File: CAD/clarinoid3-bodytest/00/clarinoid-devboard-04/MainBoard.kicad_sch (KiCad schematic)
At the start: 27 parts, among them J12 I2C HEADER main to LH, J13 ENC_HEADER main to lh, J15 StereoPot_SW_CommonAudioGND, J16 AudioOut, J19 header_ws2812 main to LH, J7 I2C HEADER main to PITCH, J9 OLED_HEADER, SW1 sw_program, U2 APCI0108-P001A Teensy_4.0_Mic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, U3 Micromod outline

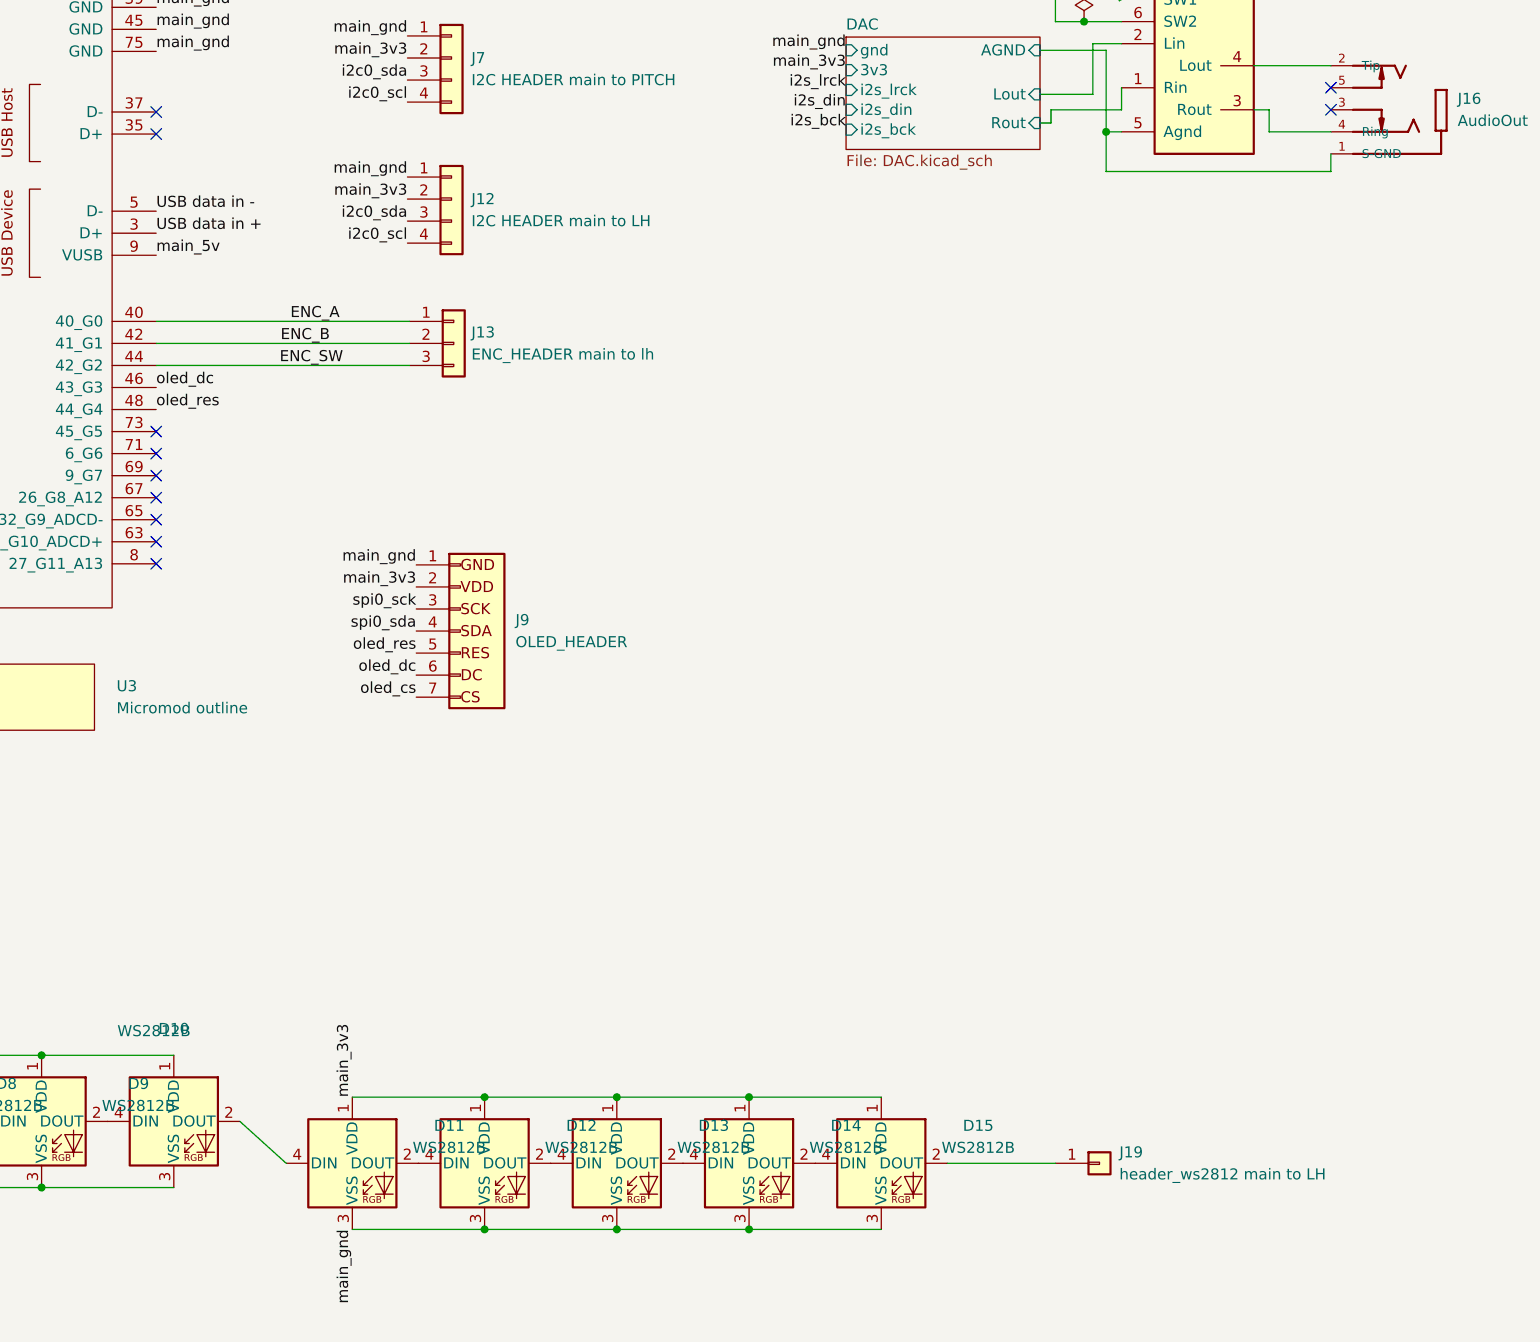
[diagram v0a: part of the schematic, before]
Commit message: adding a hardware layout sketch to the midi performer device PCB progress on the clarinoid3 body
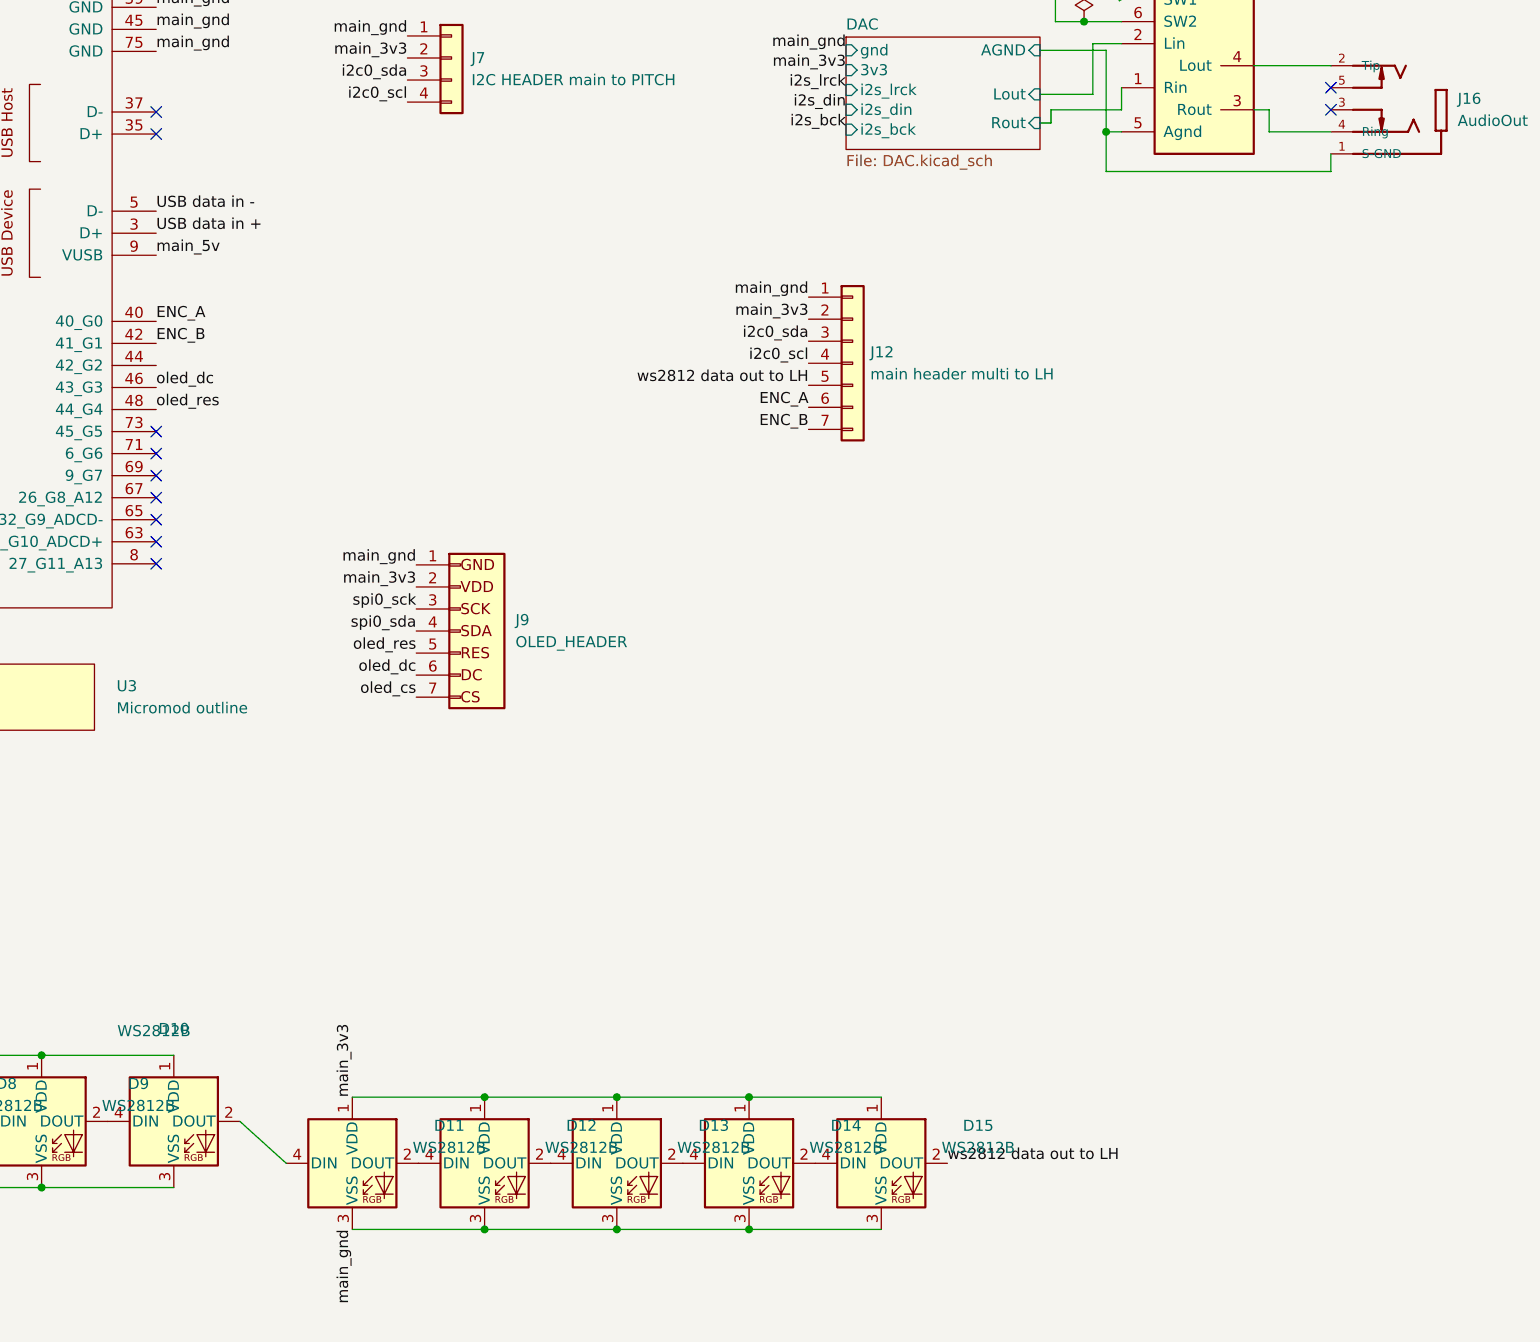
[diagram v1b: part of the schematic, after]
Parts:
- removed J12: I2C HEADER main to LH, Connector_PinHeader_2.00mm:PinHeader_1x04_P2.00mm_Vertical, symbol Connector_Generic:Conn_01x04
- removed J13: ENC_HEADER main to lh, Connector_PinHeader_2.00mm:PinHeader_1x03_P2.00mm_Vertical, symbol Connector_Generic:Conn_01x03
- removed J19: header_ws2812 main to LH, Connector_PinHeader_2.00mm:PinHeader_1x01_P2.00mm_Vertical, symbol Connector_Generic:Conn_01x01
- added J12: main header multi to LH, Connector_PinHeader_2.54mm:PinHeader_1x07_P2.54mm_Vertical, symbol Connector_Generic:Conn_01x07
- H4, H5, H6, H7: footprint clarinoid2:Wurth Elektronik Reverse SMD Spacer M3 -> MountingHole:MountingHole_2.7mm_M2.5
- J7: footprint Connector_PinHeader_2.00mm:PinHeader_1x04_P2.00mm_Vertical -> Connector_PinHeader_2.54mm:PinHeader_1x04_P2.54mm_Vertical
- J9: footprint Connector_PinHeader_2.00mm:PinHeader_1x07_P2.00mm_Vertical -> Connector_PinHeader_2.54mm:PinHeader_1x07_P2.54mm_Vertical
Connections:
- net ENC_A: now also J12.6 (Pin_6)
- net ENC_B: now also J12.7 (Pin_7)
- net i2c0_scl: now also J12.4 (Pin_4)
- net i2c0_sda: now also J12.3 (Pin_3)
- net main_3v3: now also J12.2 (Pin_2)
- net main_gnd: now also J12.1 (Pin_1)
- net ws2812 data out to LH: now reaches D15.2 (DOUT)
- net ws2812 data out to LH: now also J12.5 (Pin_5)
- net ENC_SW: no longer names the net of U2.44 (42_G2)
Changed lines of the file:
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@@
-    (stroke (width 0) (type default) (color 0 0 0 0))
-  )
-  (wire (pts (xy 142.494 144.272) (xy 113.284 144.272))
     (stroke (width 0) (type default) (color 0 0 0 0))
   )
@@
     (stroke (width 0) (type default) (color 0 0 0 0))
   )
-  (wire (pts (xy 142.494 139.192) (xy 113.284 139.192))
-    (stroke (width 0) (type default) (color 0 0 0 0))
-  )
   (wire (pts (xy 37.084 90.043) (xy 37.084 93.345))
     (stroke (width 0) (type default) (color 0 0 0 0))
@@
     (stroke (width 0) (type default) (color 0 0 0 0))
   )
-  (wire (pts (xy 216.916 236.22) (xy 204.47 236.22))
-    (stroke (width 0) (type default) (color 0 0 0 0))
-  )
   (wire (pts (xy 222.758 117.348) (xy 222.758 121.92))
     (stroke (width 0) (type default) (color 0 0 0 0))
@@
   )
   (wire (pts (xy 100.076 239.014) (xy 115.316 239.014))
-    (stroke (width 0) (type default) (color 0 0 0 0))
-  )
-  (wire (pts (xy 142.494 141.732) (xy 113.284 141.732))
     (stroke (width 0) (type default) (color 0 0 0 0))
   )
@@
     (effects (font (size 1.27 1.27)) (justify left bottom))
   )
-  (label "i2c0_scl" (at 142.24 130.175 180)
+  (label "i2c0_scl" (at 188.468 144.018 180)
     (effects (font (size 1.27 1.27)) (justify right bottom))
   )
@@
     (effects (font (size 1.27 1.27)) (justify right bottom))
   )
+  (label "ws2812 data out to LH" (at 188.468 146.558 180)
+    (effects (font (size 1.27 1.27)) (justify right bottom))
+  )
   (label "i2s_bck" (at 192.786 117.094 180)
     (effects (font (size 1.27 1.27)) (justify right bottom))
@@
     (effects (font (size 1.27 1.27)) (justify right bottom))
   )
-  (label "ENC_B" (at 127.6189 141.732 0)
+  (label "ENC_A" (at 188.468 149.098 180)
+    (effects (font (size 1.27 1.27)) (justify right bottom))
+  )
+  (label "ENC_B" (at 113.284 141.732 0)
     (effects (font (size 1.27 1.27)) (justify left bottom))
   )
@@
     (effects (font (size 1.27 1.27)) (justify right bottom))
   )
-  (label "main_3v3" (at 142.24 125.095 180)
+  (label "main_3v3" (at 188.468 138.938 180)
     (effects (font (size 1.27 1.27)) (justify right bottom))
   )
@@
     (effects (font (size 1.27 1.27)) (justify left bottom))
   )
+  (label "ws2812 data out to LH" (at 204.47 236.22 0)
+    (effects (font (size 1.27 1.27)) (justify left bottom))
+  )
+  (label "ENC_B" (at 188.468 151.638 180)
+    (effects (font (size 1.27 1.27)) (justify right bottom))
+  )
   (label "main_gnd" (at 242.57 79.883 180)
     (effects (font (size 1.27 1.27)) (justify right bottom))
@@
     (effects (font (size 1.27 1.27)) (justify right bottom))
   )
-  (label "ENC_A" (at 128.7493 139.192 0)
+  (label "ENC_A" (at 113.284 139.192 0)
     (effects (font (size 1.27 1.27)) (justify left bottom))
   )
@@
     (effects (font (size 1.27 1.27)) (justify right bottom))
   )
-  (label "ENC_SW" (at 127.508 144.272 0)
-    (effects (font (size 1.27 1.27)) (justify left bottom))
-  )
   (label "main_gnd" (at 105.156 27.432 180)
     (effects (font (size 1.27 1.27)) (justify right bottom))
@@
     (effects (font (size 1.27 1.27)) (justify left bottom))
   )
-  (label "main_gnd" (at 142.24 122.555 180)
+  (label "main_gnd" (at 188.468 136.398 180)
     (effects (font (size 1.27 1.27)) (justify right bottom))
   )
@@
     (effects (font (size 1.27 1.27)) (justify right bottom))
   )
-  (label "i2c0_sda" (at 142.24 127.635 180)
+  (label "i2c0_sda" (at 188.468 141.478 180)
     (effects (font (size 1.27 1.27)) (justify right bottom))
   )
@@
       (effects (font (size 1.27 1.27)) (justify left))
     )
-    (property "Footprint" "clarinoid2:Wurth Elektronik Reverse SMD Spacer M3" (id 2) (at 170.053 61.468 0)
+    (property "Footprint" "MountingHole:MountingHole_2.7mm_M2.5" (id 2) (at 170.053 61.468 0)
       (effects (font (size 1.27 1.27)) hide)
     )
@@
       (effects (font (size 1.27 1.27)) (justify left))
     )
-    (property "Footprint" "Connector_PinHeader_2.00mm:PinHeader_1x07_P2.00mm_Vertical" (id 2) (at 148.336 174.879 0)
+    (property "Footprint" "Connector_PinHeader_2.54mm:PinHeader_1x07_P2.54mm_Vertical" (id 2) (at 148.336 174.879 0)
       (effects (font (size 1.27 1.27)) hide)
     )
@@
       (effects (font (size 1.27 1.27)) (justify left))
     )
-    (property "Footprint" "clarinoid2:Wurth Elektronik Reverse SMD Spacer M3" (id 2) (at 169.418 50.673 0)
+    (property "Footprint" "MountingHole:MountingHole_2.7mm_M2.5" (id 2) (at 169.418 50.673 0)
       (effects (font (size 1.27 1.27)) hide)
     )
@@
       (effects (font (size 1.27 1.27)) hide)
     )
-  )
-  (symbol (lib_id "Connector_Generic:Conn_01x04") (at 147.32 125.095 0) (unit 1)
-    (in_bom yes) (on_board yes) (fields_autoplaced)
-    (property "Reference" "J12" (id 0) (at 149.606 125.0949 0)
-      (effects (font (size 1.27 1.27)) (justify left))
-    )
-    (property "Value" "I2C HEADER main to LH" (id 1) (at 149.606 127.6349 0)
-      (effects (font (size 1.27 1.27)) (justify left))
-    )
-    (property "Footprint" "Connector_PinHeader_2.00mm:PinHeader_1x04_P2.00mm_Vertical" (id 2) (at 147.32 125.095 0)
-      (effects (font (size 1.27 1.27)) hide)
-    )
-    (property "Datasheet" "~" (id 3) (at 147.32 125.095 0)
-      (effects (font (size 1.27 1.27)) hide)
-    )
-    (pin "1")
-    (pin "2")
-    (pin "3")
-    (pin "4")
   )
   (symbol (lib_id "clarinoid2:StereoPot_SW_CommonAudioGND") (at 229.616 109.728 0) (unit 1)
@@
       (effects (font (size 1.27 1.27)) (justify left))
     )
-    (property "Footprint" "Connector_PinHeader_2.00mm:PinHeader_1x04_P2.00mm_Vertical" (id 2) (at 147.32 108.839 0)
+    (property "Footprint" "Connector_PinHeader_2.54mm:PinHeader_1x04_P2.54mm_Vertical" (id 2) (at 147.32 108.839 0)
       (effects (font (size 1.27 1.27)) hide)
     )
@@
     (pin "4")
   )
+  (symbol (lib_id "Connector_Generic:Conn_01x07") (at 193.548 144.018 0) (unit 1)
+    (in_bom yes) (on_board yes) (fields_autoplaced)
+    (property "Reference" "J12" (id 0) (at 195.58 142.7479 0)
+      (effects (font (size 1.27 1.27)) (justify left))
+    )
+    (property "Value" "main header multi to LH" (id 1) (at 195.58 145.2879 0)
+      (effects (font (size 1.27 1.27)) (justify left))
+    )
+    (property "Footprint" "Connector_PinHeader_2.54mm:PinHeader_1x07_P2.54mm_Vertical" (id 2) (at 193.548 144.018 0)
+      (effects (font (size 1.27 1.27)) hide)
+    )
+    (property "Datasheet" "~" (id 3) (at 193.548 144.018 0)
+      (effects (font (size 1.27 1.27)) hide)
+    )
+    (pin "1")
+    (pin "2")
+    (pin "3")
+    (pin "4")
+    (pin "5")
+    (pin "6")
+    (pin "7")
+  )
   (symbol (lib_id "Mechanical:MountingHole") (at 171.323 71.628 0) (unit 1)
     (in_bom no) (on_board yes) (fields_autoplaced)
@@
       (effects (font (size 1.27 1.27)) (justify left))
     )
-    (property "Footprint" "clarinoid2:Wurth Elektronik Reverse SMD Spacer M3" (id 2) (at 171.323 71.628 0)
+    (property "Footprint" "MountingHole:MountingHole_2.7mm_M2.5" (id 2) (at 171.323 71.628 0)
       (effects (font (size 1.27 1.27)) hide)
     )
@@
     (pin "4")
   )
-  (symbol (lib_id "Connector_Generic:Conn_01x01") (at 221.996 236.22 0) (unit 1)
-    (in_bom yes) (on_board yes) (fields_autoplaced)
-    (property "Reference" "J19" (id 0) (at 224.282 234.9499 0)
-      (effects (font (size 1.27 1.27)) (justify left))
-    )
-    (property "Value" "header_ws2812 main to LH" (id 1) (at 224.282 237.4899 0)
-      (effects (font (size 1.27 1.27)) (justify left))
-    )
-    (property "Footprint" "Connector_PinHeader_2.00mm:PinHeader_1x01_P2.00mm_Vertical" (id 2) (at 221.996 236.22 0)
-      (effects (font (size 1.27 1.27)) hide)
-    )
-    (property "Datasheet" "~" (id 3) (at 221.996 236.22 0)
-      (effects (font (size 1.27 1.27)) hide)
-    )
-    (pin "1")
-  )
   (symbol (lib_id "clarinoid2:Placeholder") (at 97.282 181.229 0) (unit 1)
     (in_bom no) (on_board yes) (fields_autoplaced)
@@
     )
   )
-  (symbol (lib_id "Connector_Generic:Conn_01x03") (at 147.574 141.732 0) (unit 1)
-    (in_bom yes) (on_board yes) (fields_autoplaced)
-    (property "Reference" "J13" (id 0) (at 149.606 140.4619 0)
-      (effects (font (size 1.27 1.27)) (justify left))
-    )
-    (property "Value" "ENC_HEADER main to lh" (id 1) (at 149.606 143.0019 0)
-      (effects (font (size 1.27 1.27)) (justify left))
-    )
-    (property "Footprint" "Connector_PinHeader_2.00mm:PinHeader_1x03_P2.00mm_Vertical" (id 2) (at 147.574 141.732 0)
-      (effects (font (size 1.27 1.27)) hide)
-    )
-    (property "Datasheet" "~" (id 3) (at 147.574 141.732 0)
-      (effects (font (size 1.27 1.27)) hide)
-    )
-    (pin "1")
-    (pin "2")
-    (pin "3")
-  )
   (symbol (lib_id "LED:WS2812B") (at 196.85 236.22 0) (unit 1)
     (in_bom yes) (on_board yes) (fields_autoplaced)
@@
       (effects (font (size 1.27 1.27)) (justify left))
     )
-    (property "Footprint" "clarinoid2:Wurth Elektronik Reverse SMD Spacer M3" (id 2) (at 172.593 85.598 0)
-      (effects (font (size 1.27 1.27)) hide)
-    )
+    (property "Footprint" "MountingHole:MountingHole_2.7mm_M2.5" (id 2) (at 172.593 85.598 0)
+      (effects (font (size 1.27 1.27)) hide)
+    )
